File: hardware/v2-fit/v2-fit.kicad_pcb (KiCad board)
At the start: 2 copper layers, 37.9 x 23.6 mm, 24 parts, among them J2 D0-D5 GND, U1 XIAO ESP32-C6 socket

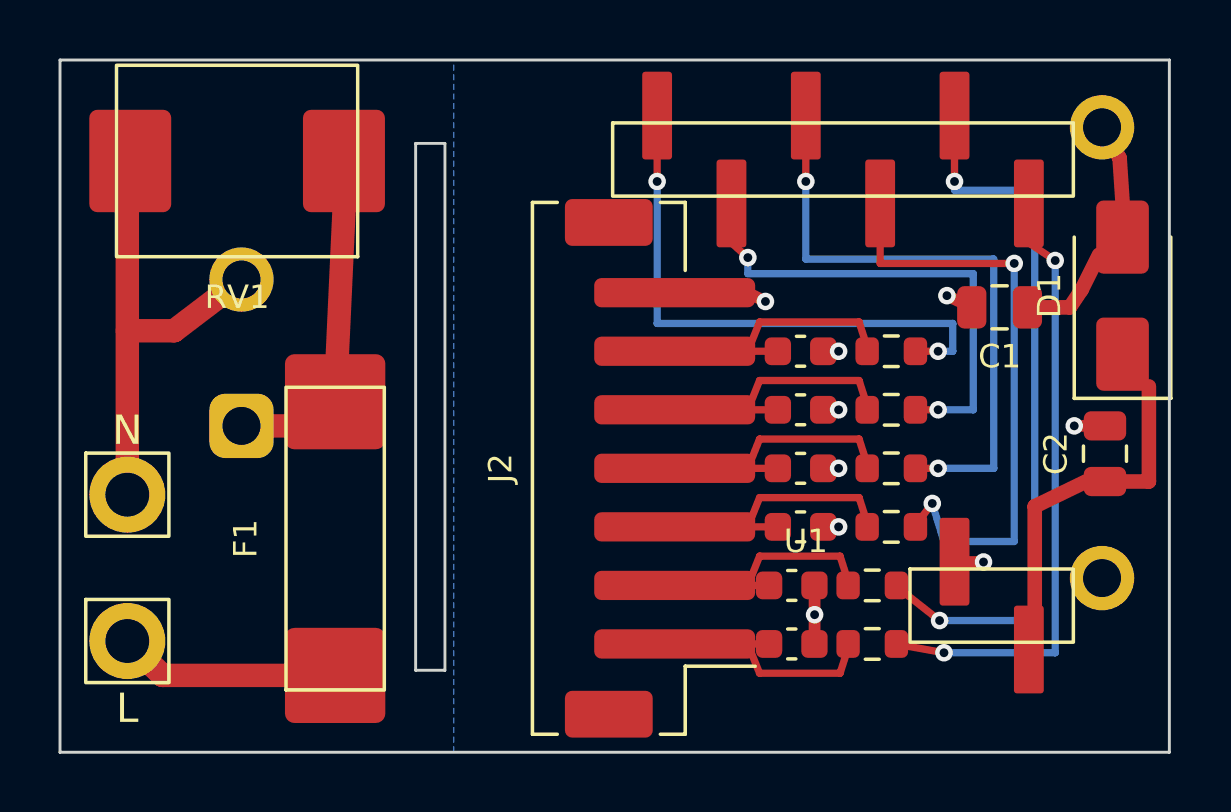
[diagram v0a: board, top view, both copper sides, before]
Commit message: Hardware: v2 silkscreen in the console site's style
Label J2's contacts, draw plain references with no panel suffix, and
keep all silk clear of pads, vias and holes. Add the mains warning and
the uncertified mark on the board, so they stay once the rails are off.
The panel rails get the grid, a ruler, the setup steps and a side view.

Copper, BOM and CPL are unchanged. Local work, not approved for ordering.

Co-Authored-By: Claude Opus 5.5 <noreply@anthropic.com>
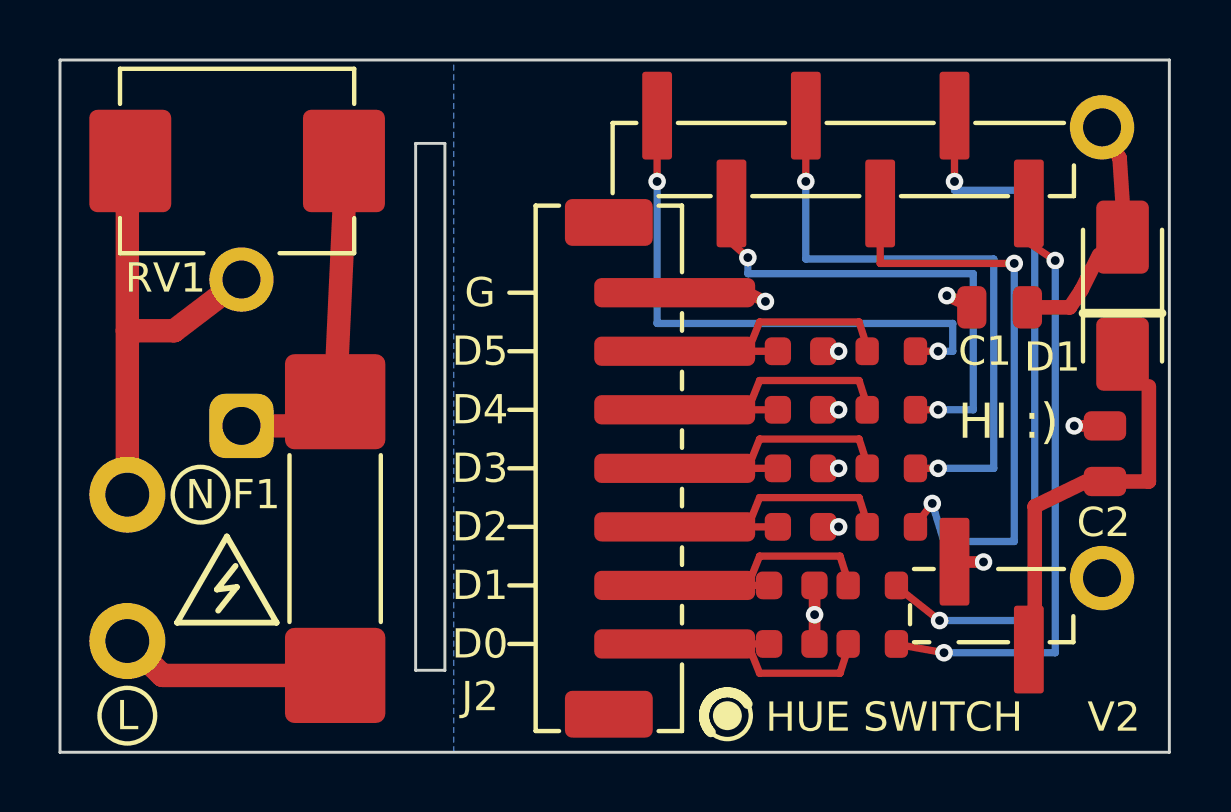
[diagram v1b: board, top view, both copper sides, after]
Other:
- board text added: "220V AC"
- board text added: "C1"
- board text added: "C2"
- board text added: "D0"
- board text added: "D1"
- board text added: "D2"
- board text added: "D3"
- board text added: "D4"
- board text added: "D5"
- board text added: "F1"
- board text added: "G"
- board text added: "HI :)"
- board text added: "HUE SWITCH"
- board text added: "J2"
- board text added: "RV1"
- board text added: "UNCERTIFIED PROTOTYPE"
- board text added: "V2"

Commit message: Hardware: v2 fixes from the two independent reviews
Stop the build on isolation errors and on any rule that does not fire,
on the board and on the panel. Stop the creepage rule reporting rule
areas and mouse bites. Count J2's tabs, copper with no net, in
measure.py. Add XIAO insertion marks to the silkscreen and the assembly
steps to REPORT.md. Copper, BOM and CPL are unchanged.

Co-Authored-By: Claude Opus 5.5 <noreply@anthropic.com>
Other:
- board text added: "5V"
- board text added: "GND"
- board text added: "USB"
